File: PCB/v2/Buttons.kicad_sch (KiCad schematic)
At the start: 20 parts

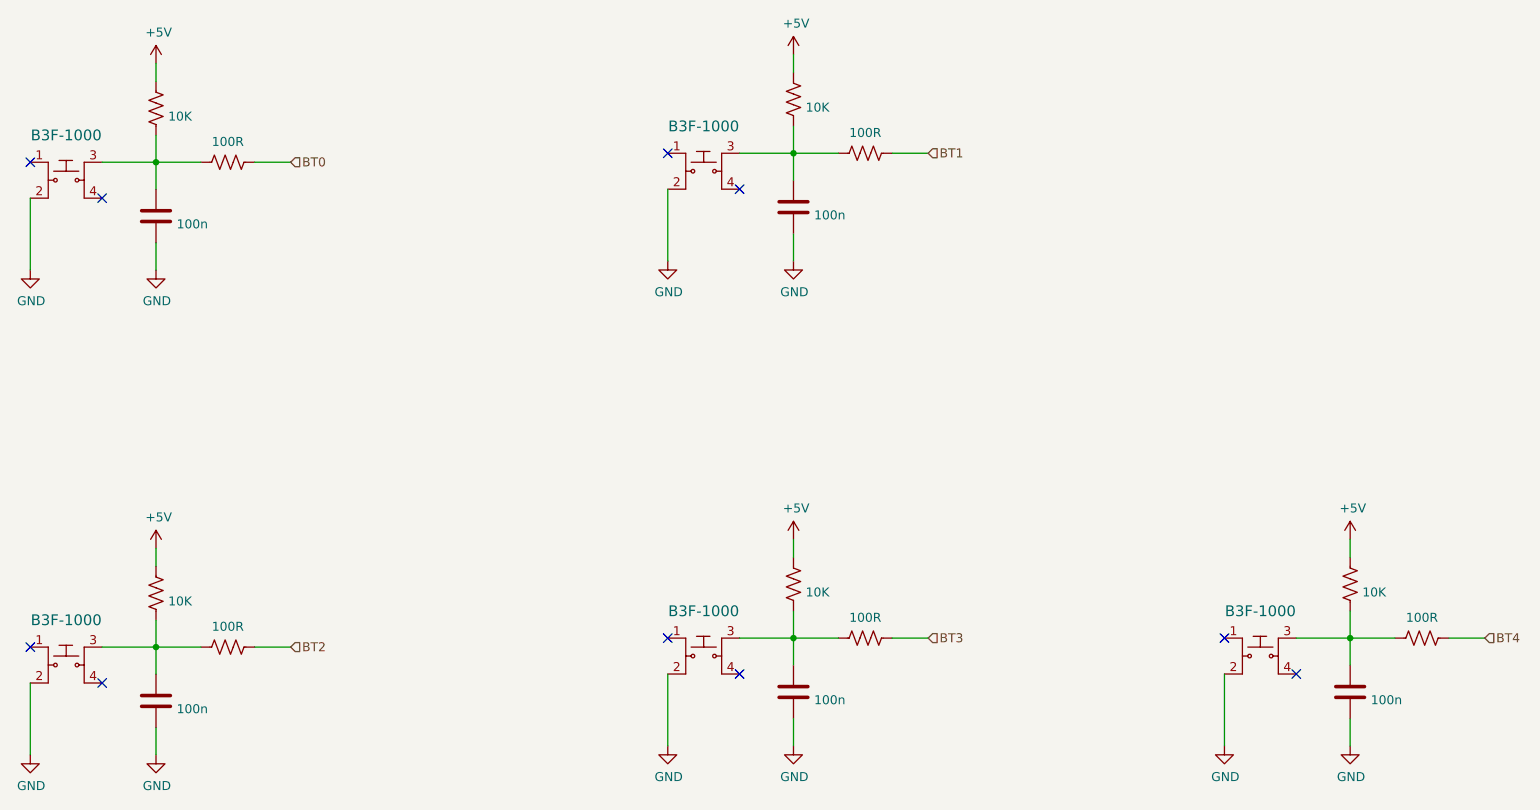
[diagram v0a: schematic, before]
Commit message: WIP updated symbols for tmc5106
Updated footprint for tmc5106,
need to check how motor wiring is done, might be wired up stupid before and that's gonna be sad
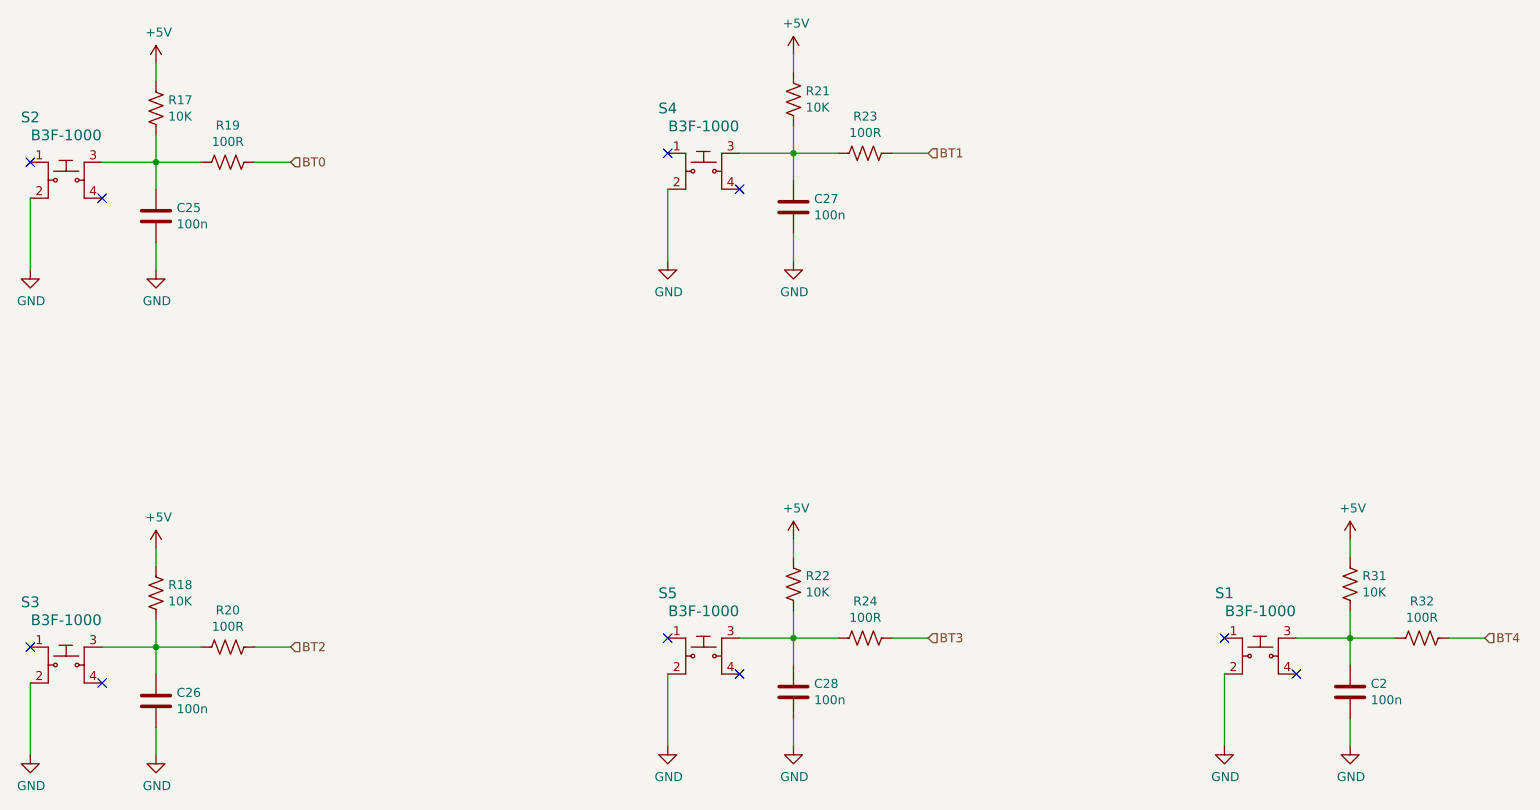
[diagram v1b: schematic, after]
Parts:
- gave numbers to parts that had none: 20
